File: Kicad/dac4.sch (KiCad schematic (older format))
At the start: 10 parts

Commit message: Fixing some review comments.
* PCB has rounded corners.
* Add JLCPCB part numbers for SMT parts
* Fixed Fab layer
* Renumbered Slots
* Mounting holes do not have thermal relief

Closes #13 #12 and #10
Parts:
- R501, R502, R504, R506, R508: LCSC Part# (none) -> C17575
- R503, R505, R507, R509: LCSC Part# (none) -> C97163
- R510: LCSC Part# (none) -> C79483
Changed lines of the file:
@@
 $Descr A4 11693 8268
 encoding utf-8
-Sheet 14 11
+Sheet 7 11
 Title "Neotron Common Hardware - 4-bit DAC"
 Date "2021-06-03"
@@
 F 6 "RNCF0805DTE24K0" H 3500 2700 50  0001 C CNN "MPN"
 F 7 "Stackpole" H 3500 2700 50  0001 C CNN "Manufacturer"
+F 8 "C17575" H 3500 2700 50  0001 C CNN "LCSC Part#"
 	1    3500 2700
 	1    0    0    -1
@@
 F 6 "RNCF0805DTE12K0" H 4000 3000 50  0001 C CNN "MPN"
 F 7 "Stackpole" H 4000 3000 50  0001 C CNN "Manufacturer"
+F 8 "C97163" H 4000 3000 50  0001 C CNN "LCSC Part#"
 	1    4000 3000
 	0    1    1    0
@@
 F 6 "RNCF0805DTE24K0" H 4500 2700 50  0001 C CNN "MPN"
 F 7 "Stackpole" H 4500 2700 50  0001 C CNN "Manufacturer"
+F 8 "C17575" H 4500 2700 50  0001 C CNN "LCSC Part#"
 	1    4500 2700
 	1    0    0    -1
@@
 F 6 "RNCF0805DTE12K0" H 5000 3000 50  0001 C CNN "MPN"
 F 7 "Stackpole" H 5000 3000 50  0001 C CNN "Manufacturer"
+F 8 "C97163" H 5000 3000 50  0001 C CNN "LCSC Part#"
 	1    5000 3000
 	0    1    1    0
@@
 F 6 "RNCF0805DTE12K0" H 6000 3000 50  0001 C CNN "MPN"
 F 7 "Stackpole" H 6000 3000 50  0001 C CNN "Manufacturer"
+F 8 "C97163" H 6000 3000 50  0001 C CNN "LCSC Part#"
 	1    6000 3000
 	0    1    1    0
@@
 F 6 "RNCF0805DTE12K0" H 7000 3000 50  0001 C CNN "MPN"
 F 7 "Stackpole" H 7000 3000 50  0001 C CNN "Manufacturer"
+F 8 "C97163" H 7000 3000 50  0001 C CNN "LCSC Part#"
 	1    7000 3000
 	0    1    1    0
@@
 F 6 "RNCF0805DTE3K48" H 7550 3300 50  0001 C CNN "MPN"
 F 7 "Stackpole" H 7550 3300 50  0001 C CNN "Manufacturer"
+F 8 "C79483" H 7550 3300 50  0001 C CNN "LCSC Part#"
 	1    7550 3300
 	1    0    0    -1
@@
 F 6 "RNCF0805DTE24K0" H 3500 3300 50  0001 C CNN "MPN"
 F 7 "Stackpole" H 3500 3300 50  0001 C CNN "Manufacturer"
+F 8 "C17575" H 3500 3300 50  0001 C CNN "LCSC Part#"
 	1    3500 3300
 	1    0    0    -1
@@
 F 6 "RNCF0805DTE24K0" H 5500 2700 50  0001 C CNN "MPN"
 F 7 "Stackpole" H 5500 2700 50  0001 C CNN "Manufacturer"
+F 8 "C17575" H 5500 2700 50  0001 C CNN "LCSC Part#"
 	1    5500 2700
 	1    0    0    -1
@@
 F 6 "RNCF0805DTE24K0" H 6500 2700 50  0001 C CNN "MPN"
 F 7 "Stackpole" H 6500 2700 50  0001 C CNN "Manufacturer"
+F 8 "C17575" H 6500 2700 50  0001 C CNN "LCSC Part#"
 	1    6500 2700
 	1    0    0    -1

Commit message: BoM and PCB fixes.
* Move tolerances and voltages out of value and into their own fields.
* Fix 5V trace for audio stage.
* Fixup docs.yml so outputs work for JLCPCB.
* Fix JLCPCB part number for 22pF caps.
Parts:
- R501, R502, R504, R506, R508: value 24k 0.5% -> 24k; Tolerance (none) -> 0.5%
- R503, R505, R507, R509: value 12k 0.5% -> 12k; Tolerance (none) -> 0.5%
- R510: value 3480 0.5% -> 3480; Tolerance (none) -> 0.5%
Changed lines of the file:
@@
 AR Path="/60687F8A/600A04B7/5F5F4D05" Ref="R701"  Part="1"
 F 0 "R701" H 3570 2746 50  0000 L CNN
-F 1 "24k 0.5%" H 3570 2655 50  0000 L CNN
+F 1 "24k" H 3570 2655 50  0000 L CNN
 F 2 "Resistor_SMD:R_0805_2012Metric_Pad1.20x1.40mm_HandSolder" V 3430 2700 50  0001 C CNN
 F 3 "~" H 3500 2700 50  0001 C CNN
@@
 F 7 "Stackpole" H 3500 2700 50  0001 C CNN "Manufacturer"
 F 8 "C17575" H 3500 2700 50  0001 C CNN "LCSC Part#"
+F 9 "0.5%" H 3500 2700 50  0001 C CNN "Tolerance"
 	1    3500 2700
 	1    0    0    -1
@@
 AR Path="/60687F8A/600A04B7/60681FF9" Ref="R703"  Part="1"
 F 0 "R703" V 4100 3000 50  0000 C CNN
-F 1 "12k 0.5%" V 4200 3000 50  0000 C CNN
+F 1 "12k" V 4200 3000 50  0000 C CNN
 F 2 "Resistor_SMD:R_0805_2012Metric_Pad1.20x1.40mm_HandSolder" V 3930 3000 50  0001 C CNN
 F 3 "~" H 4000 3000 50  0001 C CNN
@@
 F 7 "Stackpole" H 4000 3000 50  0001 C CNN "Manufacturer"
 F 8 "C97163" H 4000 3000 50  0001 C CNN "LCSC Part#"
+F 9 "0.5%" H 4000 3000 50  0001 C CNN "Tolerance"
 	1    4000 3000
 	0    1    1    0
@@
 AR Path="/60687F8A/600A04B7/60681FFA" Ref="R704"  Part="1"
 F 0 "R704" H 4570 2746 50  0000 L CNN
-F 1 "24k 0.5%" H 4570 2655 50  0000 L CNN
+F 1 "24k" H 4570 2655 50  0000 L CNN
 F 2 "Resistor_SMD:R_0805_2012Metric_Pad1.20x1.40mm_HandSolder" V 4430 2700 50  0001 C CNN
 F 3 "~" H 4500 2700 50  0001 C CNN
@@
 F 7 "Stackpole" H 4500 2700 50  0001 C CNN "Manufacturer"
 F 8 "C17575" H 4500 2700 50  0001 C CNN "LCSC Part#"
+F 9 "0.5%" H 4500 2700 50  0001 C CNN "Tolerance"
 	1    4500 2700
 	1    0    0    -1
@@
 AR Path="/60687F8A/600A04B7/60681FFB" Ref="R705"  Part="1"
 F 0 "R705" V 5100 3000 50  0000 C CNN
-F 1 "12k 0.5%" V 5200 3000 50  0000 C CNN
+F 1 "12k" V 5200 3000 50  0000 C CNN
 F 2 "Resistor_SMD:R_0805_2012Metric_Pad1.20x1.40mm_HandSolder" V 4930 3000 50  0001 C CNN
 F 3 "~" H 5000 3000 50  0001 C CNN
@@
 F 7 "Stackpole" H 5000 3000 50  0001 C CNN "Manufacturer"
 F 8 "C97163" H 5000 3000 50  0001 C CNN "LCSC Part#"
+F 9 "0.5%" H 5000 3000 50  0001 C CNN "Tolerance"
 	1    5000 3000
 	0    1    1    0
@@
 AR Path="/60687F8A/600A04B7/60681FFC" Ref="R707"  Part="1"
 F 0 "R707" V 6100 3000 50  0000 C CNN
-F 1 "12k 0.5%" V 6200 3000 50  0000 C CNN
+F 1 "12k" V 6200 3000 50  0000 C CNN
 F 2 "Resistor_SMD:R_0805_2012Metric_Pad1.20x1.40mm_HandSolder" V 5930 3000 50  0001 C CNN
 F 3 "~" H 6000 3000 50  0001 C CNN
@@
 F 7 "Stackpole" H 6000 3000 50  0001 C CNN "Manufacturer"
 F 8 "C97163" H 6000 3000 50  0001 C CNN "LCSC Part#"
+F 9 "0.5%" H 6000 3000 50  0001 C CNN "Tolerance"
 	1    6000 3000
 	0    1    1    0
@@
 AR Path="/60687F8A/600A04B7/60681FFD" Ref="R709"  Part="1"
 F 0 "R709" V 7100 3000 50  0000 C CNN
-F 1 "12k 0.5%" V 7200 3000 50  0000 C CNN
+F 1 "12k" V 7200 3000 50  0000 C CNN
 F 2 "Resistor_SMD:R_0805_2012Metric_Pad1.20x1.40mm_HandSolder" V 6930 3000 50  0001 C CNN
 F 3 "~" H 7000 3000 50  0001 C CNN
@@
 F 7 "Stackpole" H 7000 3000 50  0001 C CNN "Manufacturer"
 F 8 "C97163" H 7000 3000 50  0001 C CNN "LCSC Part#"
+F 9 "0.5%" H 7000 3000 50  0001 C CNN "Tolerance"
 	1    7000 3000
 	0    1    1    0
@@
 AR Path="/60687F8A/600A04B7/60681FFF" Ref="R710"  Part="1"
 F 0 "R710" H 7620 3346 50  0000 L CNN
-F 1 "3480 0.5%" H 7620 3255 50  0000 L CNN
+F 1 "3480" H 7620 3255 50  0000 L CNN
 F 2 "Resistor_SMD:R_0805_2012Metric_Pad1.20x1.40mm_HandSolder" V 7480 3300 50  0001 C CNN
 F 3 "~" H 7550 3300 50  0001 C CNN
@@
 F 7 "Stackpole" H 7550 3300 50  0001 C CNN "Manufacturer"
 F 8 "C79483" H 7550 3300 50  0001 C CNN "LCSC Part#"
+F 9 "0.5%" H 7550 3300 50  0001 C CNN "Tolerance"
 	1    7550 3300
 	1    0    0    -1
@@
 AR Path="/60687F8A/600A04B7/60682002" Ref="R702"  Part="1"
 F 0 "R702" H 3570 3346 50  0000 L CNN
-F 1 "24k 0.5%" H 3570 3255 50  0000 L CNN
+F 1 "24k" H 3570 3255 50  0000 L CNN
 F 2 "Resistor_SMD:R_0805_2012Metric_Pad1.20x1.40mm_HandSolder" V 3430 3300 50  0001 C CNN
 F 3 "~" H 3500 3300 50  0001 C CNN
@@
 F 7 "Stackpole" H 3500 3300 50  0001 C CNN "Manufacturer"
 F 8 "C17575" H 3500 3300 50  0001 C CNN "LCSC Part#"
+F 9 "0.5%" H 3500 3300 50  0001 C CNN "Tolerance"
 	1    3500 3300
 	1    0    0    -1
@@
 AR Path="/60687F8A/600A04B7/60682003" Ref="R706"  Part="1"
 F 0 "R706" H 5570 2746 50  0000 L CNN
-F 1 "24k 0.5%" H 5570 2655 50  0000 L CNN
+F 1 "24k" H 5570 2655 50  0000 L CNN
 F 2 "Resistor_SMD:R_0805_2012Metric_Pad1.20x1.40mm_HandSolder" V 5430 2700 50  0001 C CNN
 F 3 "~" H 5500 2700 50  0001 C CNN
@@
 F 7 "Stackpole" H 5500 2700 50  0001 C CNN "Manufacturer"
 F 8 "C17575" H 5500 2700 50  0001 C CNN "LCSC Part#"
+F 9 "0.5%" H 5500 2700 50  0001 C CNN "Tolerance"
 	1    5500 2700
 	1    0    0    -1
@@
 AR Path="/60687F8A/600A04B7/5F5FD329" Ref="R708"  Part="1"
 F 0 "R708" H 6570 2746 50  0000 L CNN
-F 1 "24k 0.5%" H 6570 2655 50  0000 L CNN
+F 1 "24k" H 6570 2655 50  0000 L CNN
 F 2 "Resistor_SMD:R_0805_2012Metric_Pad1.20x1.40mm_HandSolder" V 6430 2700 50  0001 C CNN
 F 3 "~" H 6500 2700 50  0001 C CNN
@@
 F 7 "Stackpole" H 6500 2700 50  0001 C CNN "Manufacturer"
 F 8 "C17575" H 6500 2700 50  0001 C CNN "LCSC Part#"
+F 9 "0.5%" H 6500 2700 50  0001 C CNN "Tolerance"
 	1    6500 2700
 	1    0    0    -1

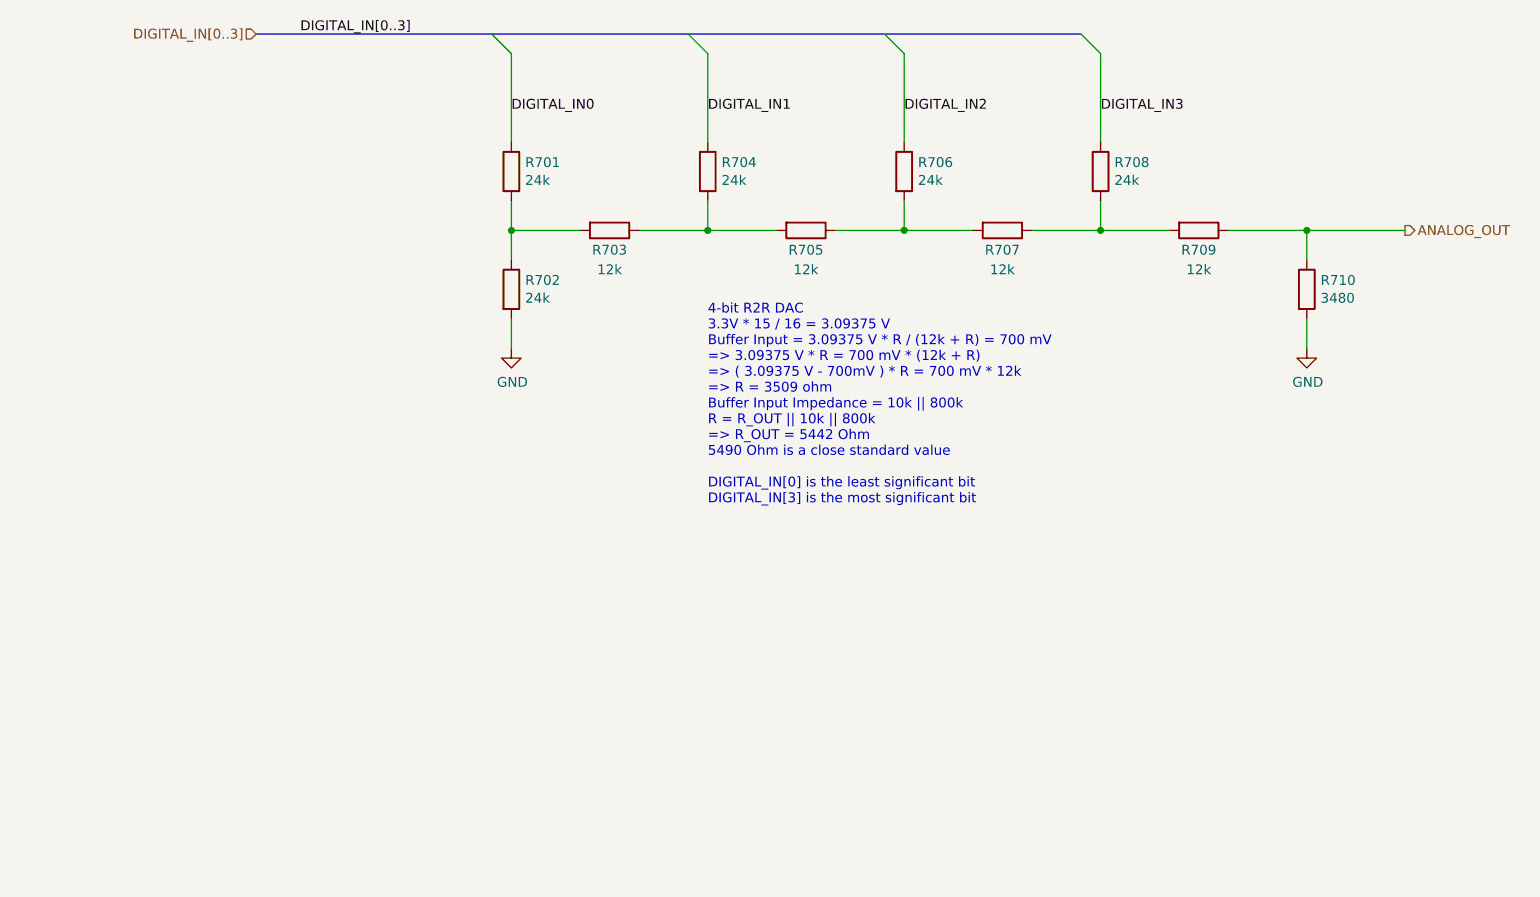
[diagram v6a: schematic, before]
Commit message: Update component values.
Tolerance and Voltage are set to the minimum acceptable. The selected
parts can be better, where a better part is cheaper or has
better availability.

Also dropped R2R DAC tolerance to 1% - 0.5% was overkill. The output
resistor had the wrong value too, which is fixed.
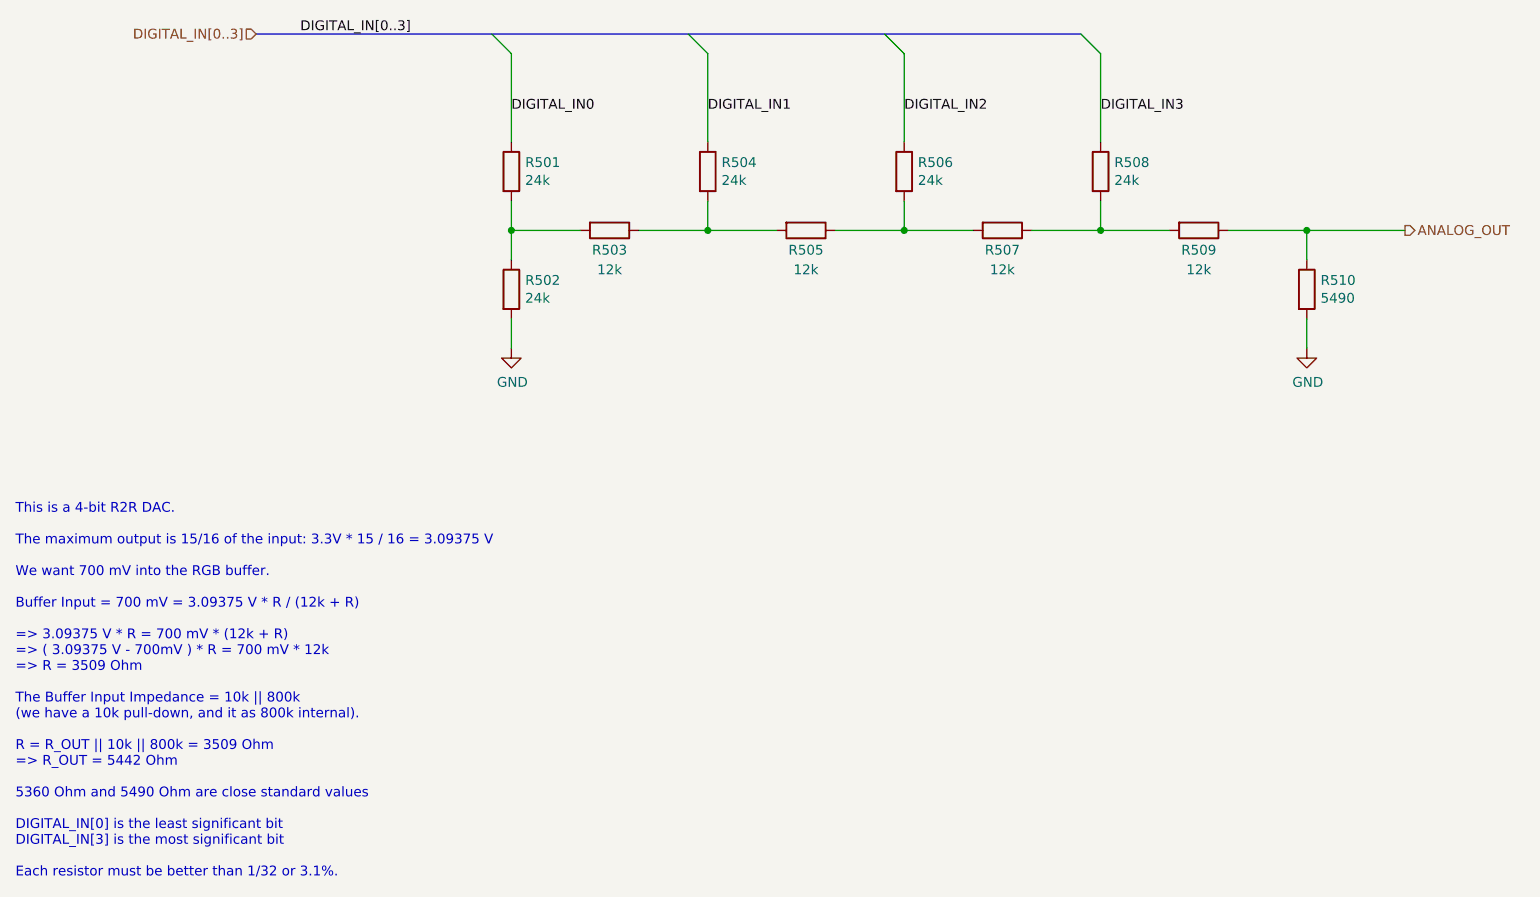
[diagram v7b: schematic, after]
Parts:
- R501, R502, R504, R506, R508: MPN RNCF0805DTE24K0 -> RMCF0805FT24K0; Tolerance 0.5% -> 1%
- R503, R505, R507, R509: MPN RNCF0805DTE12K0 -> RMCF0805FT12K0; Tolerance 0.5% -> 1%
- R510: value 3480 -> 5490; Digikey RNCF0805DTE3K48CT-ND -> RNCF0805DTE5K49CT-ND; MPN RNCF0805DTE3K48 -> RMCF0805FT5K49; Tolerance 0.5% -> 1%
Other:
- note added: "This is a 4-bit R2R DAC.\n\nThe maximum output is 15/16 of the input: 3.3V * 15 / 16 = 3.09375 V\n\nWe want 700 mV into the RGB buffer.\n\nBuffer Input = 700 mV = 3.09375 V * R / (12k + R)\n\n=> 3.09375 V * R = 700 mV * (12k + R)\n=> ( 3.09375 V - 700mV ) * R = 700 mV * 12k\n=> R = 3509 Ohm\n\nThe Buffer Input Impedance = 10k || 800k\n(we have a 10k pull-down, and it as 800k internal).\n\nR = R_O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"
- note removed: "4-bit R2R DAC\n3.3V * 15 / 16 = 3.09375 V\nBuffer Input = 3.09375 V * R / (12k + R) = 700 mV\n=> 3.09375 V * R = 700 mV * (12k + R)\n=> ( 3.09375 V - 700mV ) * R = 700 mV * 12k\n=> R = 3509 ohm\nBuffer Input Impedance = 10k || 800k\nR = R_OUT || 10k || 800k\n=> R_OUT = 5442 Ohm\n5490 Ohm is a close standard value\n\nDIGITAL_IN[0] is the least significant bit\nDIGITAL_IN[3] is the most significant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"

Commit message: Change JLCPCB part number for DAC pull-down (R510 and friends).
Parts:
- R510: LCSC Part# C79483 -> C17726
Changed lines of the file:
@@
 F 6 "RMCF0805FT5K49" H 7550 3300 50  0001 C CNN "MPN"
 F 7 "Stackpole" H 7550 3300 50  0001 C CNN "Manufacturer"
-F 8 "C79483" H 7550 3300 50  0001 C CNN "LCSC Part#"
+F 8 "C17726" H 7550 3300 50  0001 C CNN "LCSC Part#"
 F 9 "1%" H 7550 3300 50  0001 C CNN "Tolerance"
 F 10 "~" H 7550 3300 50  0001 C CNN "Voltage"
